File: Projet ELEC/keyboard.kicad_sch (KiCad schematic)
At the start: 72 parts, among them SW1 SW_TOUCHE, SW10 SW_TOUCHE, SW11 SW_TOUCHE, SW12 SW_TOUCHE, SW13 SW_TOUCHE, SW14 SW_TOUCHE, SW15 SW_TOUCHE, SW16 SW_TOUCHE, SW17 SW_TOUCHE, SW18 SW_TOUCHE, SW19 SW_TOUCHE, SW2 SW_TOUCHE, SW20 SW_TOUCHE, SW21 SW_TOUCHE, SW22 SW_TOUCHE, SW23 SW_TOUCHE, SW24 SW_TOUCHE, SW25 SW_TOUCHE, SW26 SW_TOUCHE, SW27 SW_TOUCHE, SW28 SW_TOUCHE, SW29 SW_TOUCHE, SW3 SW_TOUCHE, SW30 SW_TOUCHE, SW31 SW_TOUCHE, SW32 SW_TOUCHE, SW33 SW_TOUCHE, SW34 SW_TOUCHE, SW35 SW_TOUCHE, SW36 SW_TOUCHE, SW4 SW_TOUCHE, SW5 SW_TOUCHE, SW6 SW_TOUCHE, SW7 SW_TOUCHE, SW8 SW_TOUCHE, SW9 SW_TOUCHE

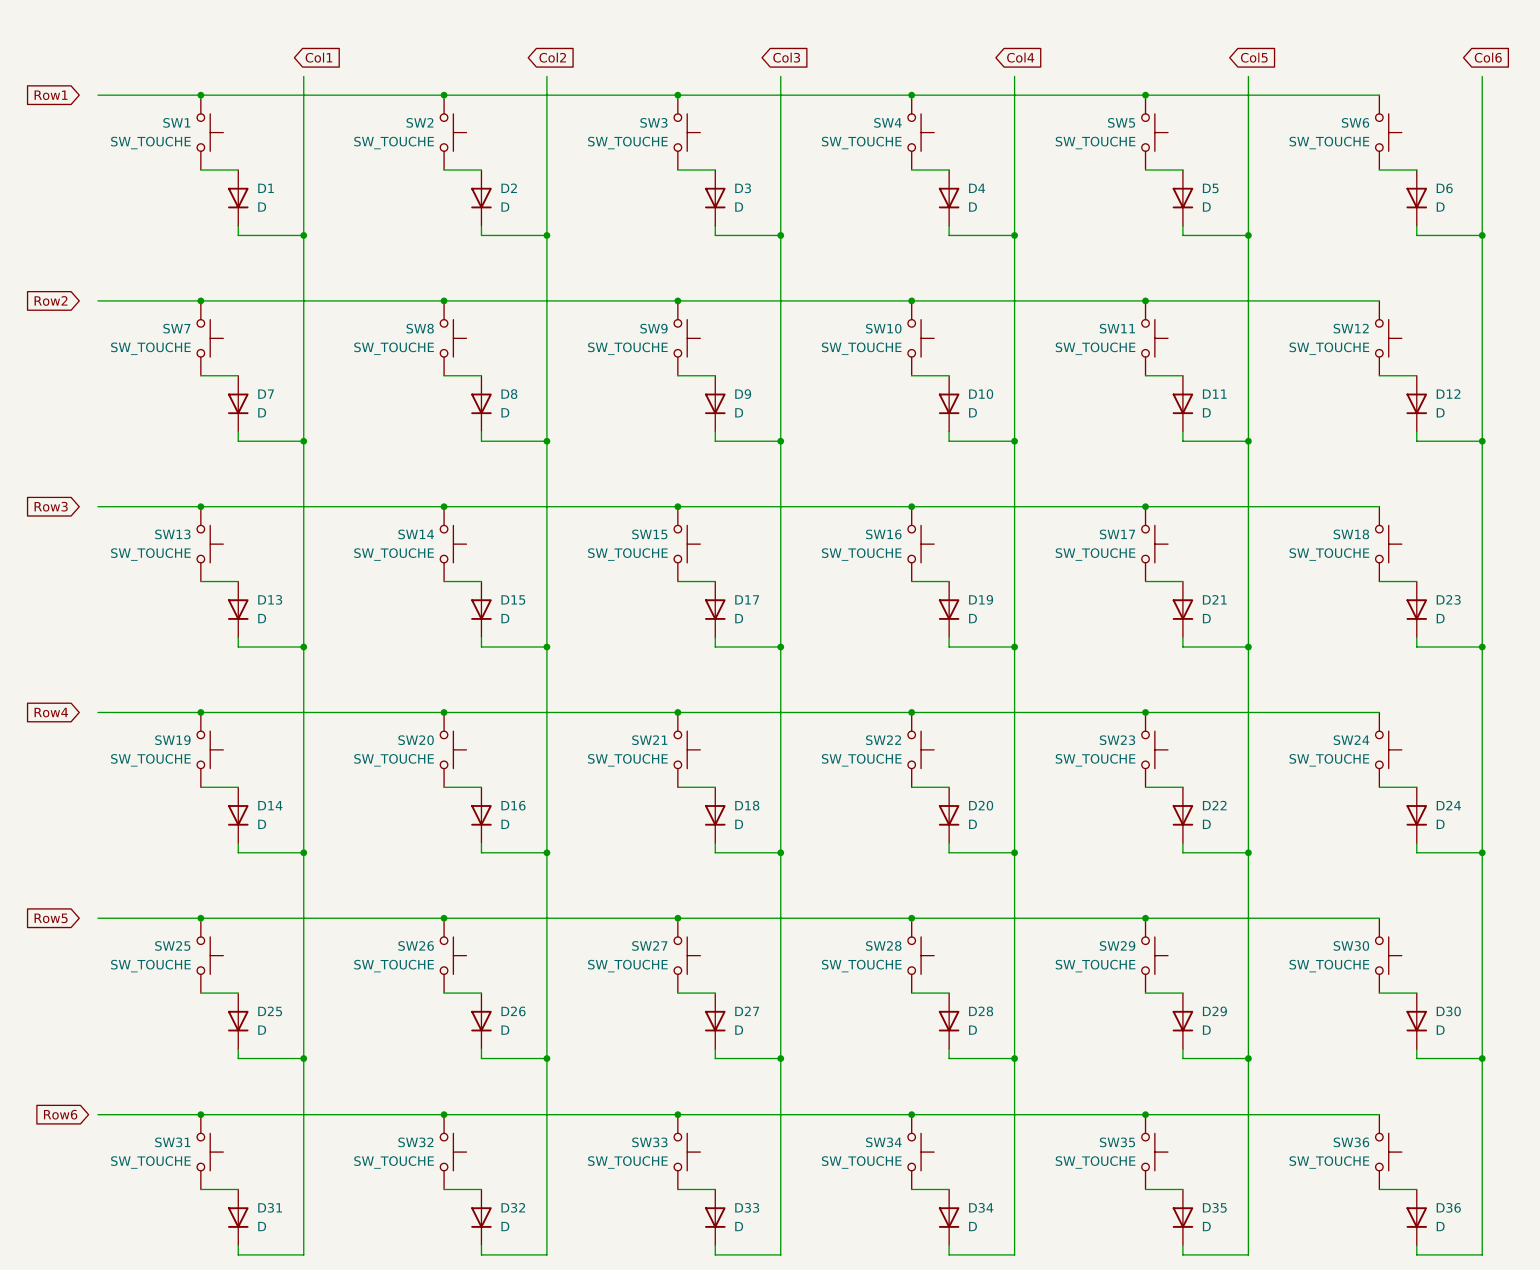
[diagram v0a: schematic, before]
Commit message: corrected around 60 errors, removed a 74ls04, and many other improvements
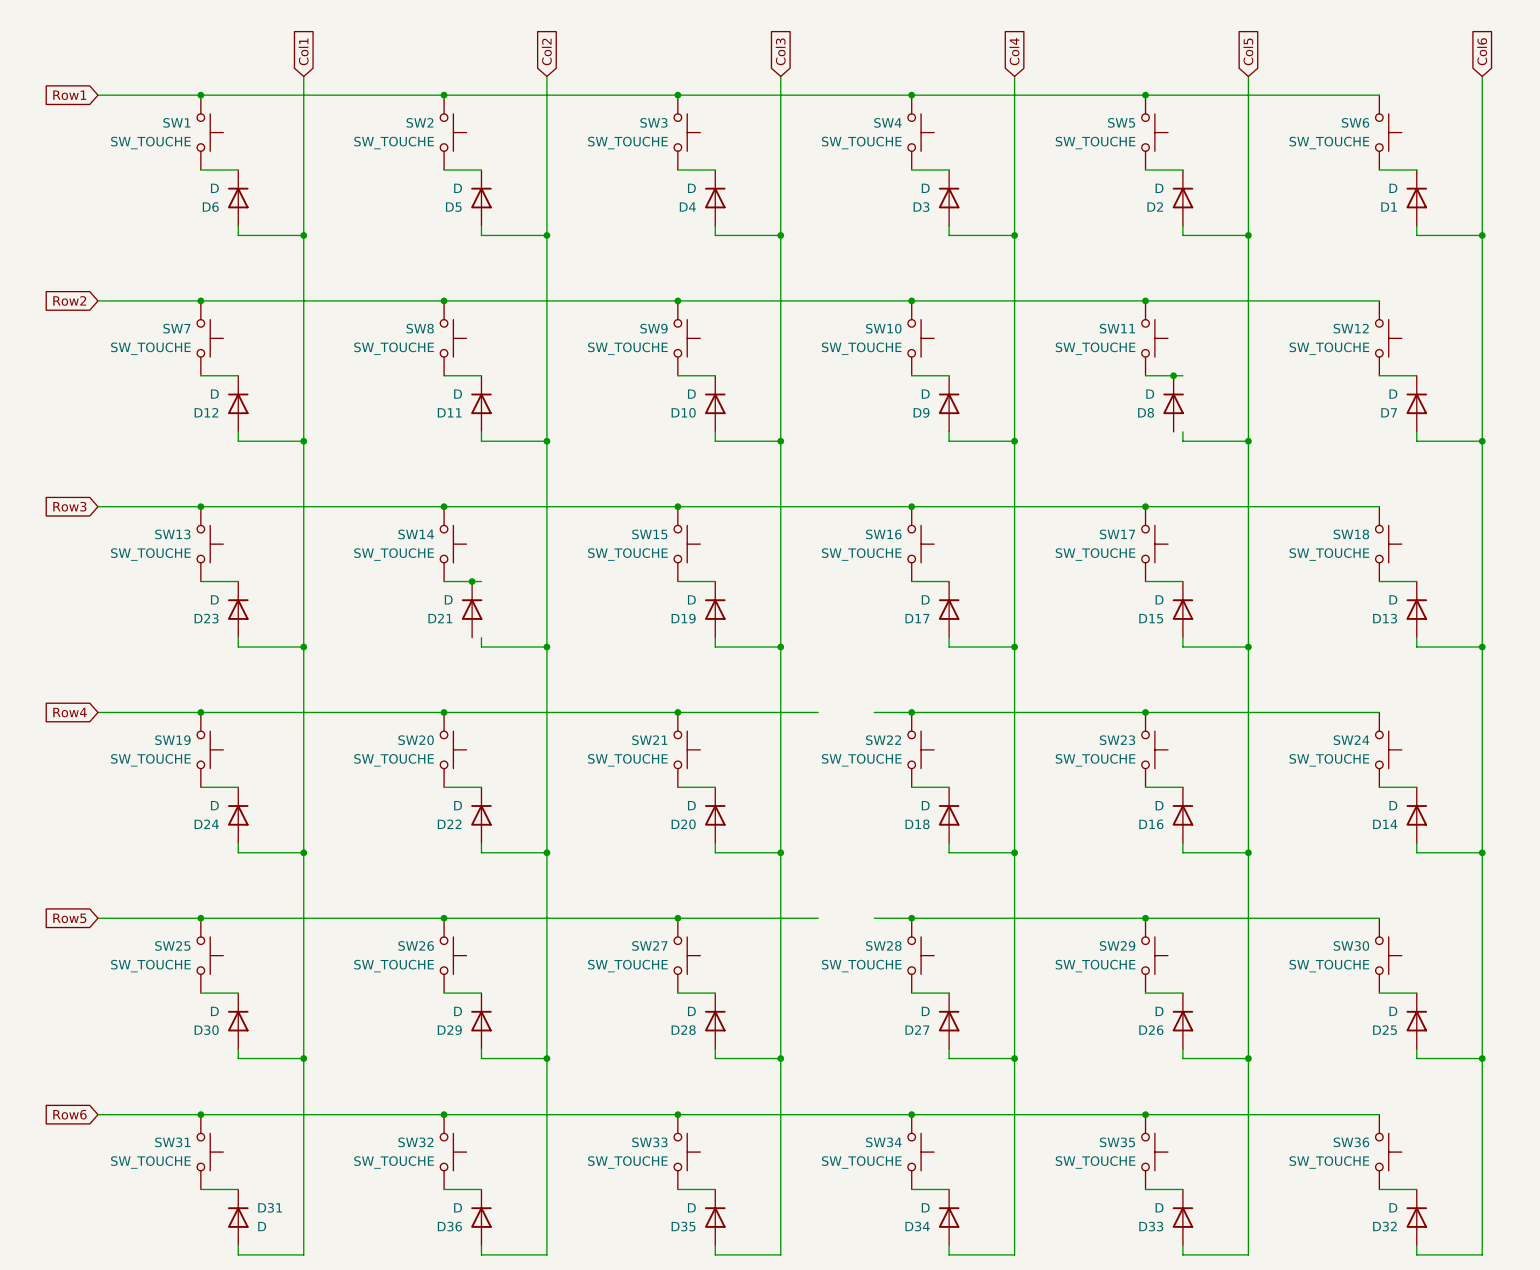
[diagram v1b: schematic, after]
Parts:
- D1, D10, D11, D12, D13, D14, D15, D16, D17, D18, D19, D2, D20, D21, D22, D23, D24, D25, D26, D27, D28, D29, D3, D30, D31, D32, D33, D34, D35, D36, D4, D5, D6, D7, D8, D9: footprint (none) -> Diode_THT:D_5W_P10.16mm_Horizontal
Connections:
- net Col1: now also D12.2 (A), D23.2 (A), D24.2 (A), D30.2 (A), D31.2 (A), D6.2 (A)
- net Col2: now also D11.2 (A), D22.2 (A), D29.2 (A), D36.2 (A), D5.2 (A)
- net Col3: now also D10.2 (A), D19.2 (A), D20.2 (A), D28.2 (A), D35.2 (A), D4.2 (A)
- net Col4: now also D17.2 (A), D18.2 (A), D27.2 (A), D3.2 (A), D34.2 (A), D9.2 (A)
- net Col5: now also D15.2 (A), D16.2 (A), D2.2 (A), D26.2 (A), D33.2 (A)
- net Col6: now also D1.2 (A), D13.2 (A), D14.2 (A), D25.2 (A), D32.2 (A), D7.2 (A)
- net Row1: now also SW1.1, SW2.1, SW3.1, SW4.1, SW5.1, SW6.1
- net Row2: now also SW10.1, SW11.1, SW12.1, SW7.1, SW8.1, SW9.1
- net Row3: now also SW13.1, SW14.1, SW15.1, SW16.1, SW17.1, SW18.1
- net Row4: now also SW19.1, SW20.1, SW21.1
- net Row5: now also SW25.1, SW26.1, SW27.1
- net Row6: now also SW31.1, SW32.1, SW33.1, SW34.1, SW35.1, SW36.1
- net at SW8.2: now also D11.1 (K); no longer D8.2 (A)
- net at SW28.1, SW29.1, SW30.1: no longer SW25.1, SW26.1, SW27.1
- net at SW26.2: now also D29.1 (K); no longer D26.2 (A)
- net at SW14.2: now also D21.1 (K); no longer D15.2 (A)
- net at SW15.2: now also D19.1 (K); no longer D17.2 (A)
- net at SW17.2: now also D15.1 (K); no longer D21.2 (A)
- net at SW35.2: now also D33.1 (K); no longer D35.2 (A)
- net at SW16.2: now also D17.1 (K); no longer D19.2 (A)
- net at SW11.2: now also D8.1 (K); no longer D11.2 (A)
- net at SW34.2: now also D34.1 (K); no longer D34.2 (A)
- net at SW9.2: now also D10.1 (K); no longer D9.2 (A)
- net at SW30.2: now also D25.1 (K); no longer D30.2 (A)
- net at SW22.1, SW23.1, SW24.1: no longer SW19.1, SW20.1, SW21.1
- net at SW22.2: now also D18.1 (K); no longer D20.2 (A)
- net at SW20.2: now also D22.1 (K); no longer D16.2 (A)
- net at SW1.2: now also D6.1 (K); no longer D1.2 (A)
- net at SW5.2: now also D2.1 (K); no longer D5.2 (A)
- net at SW21.2: now also D20.1 (K); no longer D18.2 (A)
- net at SW28.2: now also D27.1 (K); no longer D28.2 (A)
- net at SW13.2: now also D23.1 (K); no longer D13.2 (A)
- net at SW19.2: now also D24.1 (K); no longer D14.2 (A)
- net at SW31.2: now also D31.1 (K); no longer D31.2 (A)
- net at SW6.2: now also D1.1 (K); no longer D6.2 (A)
- net at SW32.2: now also D36.1 (K); no longer D32.2 (A)
- net at SW25.2: now also D30.1 (K); no longer D25.2 (A)
- net at SW3.2: now also D4.1 (K); no longer D3.2 (A)
- net at SW27.2: now also D28.1 (K); no longer D27.2 (A)
- net at SW23.2: now also D16.1 (K); no longer D22.2 (A)
- net at SW4.2: now also D3.1 (K); no longer D4.2 (A)
- net at SW24.2: now also D14.1 (K); no longer D24.2 (A)
- net at SW36.2: now also D32.1 (K); no longer D36.2 (A)
- net at SW7.2: now also D12.1 (K); no longer D7.2 (A)
- net at SW33.2: now also D35.1 (K); no longer D33.2 (A)
- net at SW2.2: now also D5.1 (K); no longer D2.2 (A)
- net at SW29.2: now also D26.1 (K); no longer D29.2 (A)
- net at SW18.2: now also D13.1 (K); no longer D23.2 (A)
- net at SW12.2: now also D7.1 (K); no longer D12.2 (A)
- net at SW10.2: now also D9.1 (K); no longer D10.2 (A)
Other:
- moved on the sheet: D1, D10, D11, D12, D13, D14, D15, D16, D17, D18, D19, D2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

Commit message: on va mourir mdr
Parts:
- D1, D10, D11, D12, D13, D14, D15, D16, D17, D18, D19, D2, D20, D21, D22, D23, D24, D25, D26, D27, D28, D29, D3, D30, D31, D32, D33, D34, D35, D36, D4, D5, D6, D7, D8, D9: footprint Diode_THT:D_5W_P10.16mm_Horizontal -> Resistor_THT:R_Axial_DIN0204_L3.6mm_D1.6mm_P5.08mm_Horizontal
- SW1, SW10, SW11, SW12, SW13, SW14, SW15, SW16, SW17, SW18, SW19, SW2, SW20, SW21, SW22, SW23, SW24, SW25, SW26, SW27, SW28, SW29, SW3, SW30, SW31, SW32, SW33, SW34, SW35, SW36, SW4, SW5, SW6, SW7, SW8, SW9: footprint Button_Switch_Keyboard:SW_Cherry_MX_1.00u_PCB -> Button_Switch_THT:SW_PUSH_6mm
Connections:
- net Col2: now also D21.2 (A)
- net Row4: now also SW22.1, SW23.1, SW24.1
- net Row5: now also SW28.1, SW29.1, SW30.1
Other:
- moved on the sheet: D21
